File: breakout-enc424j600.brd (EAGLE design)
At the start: 58.4 x 33 mm, 25 parts, among them IC1 ENC424J600-I/PT, J1 HRJACK-HR911105A

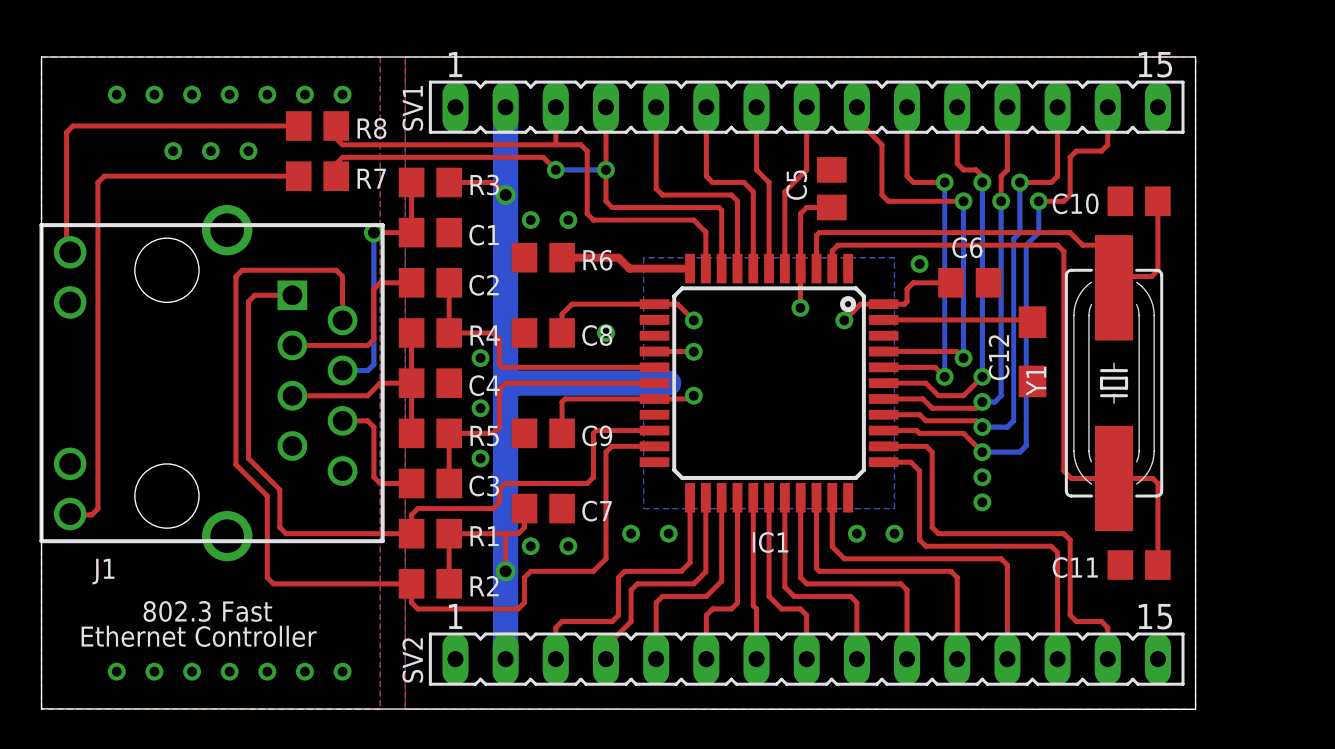
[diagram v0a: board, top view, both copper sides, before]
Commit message: Add pinout on silkscreen, change pin headers, connect ground shield on ethernet, modified board dimension
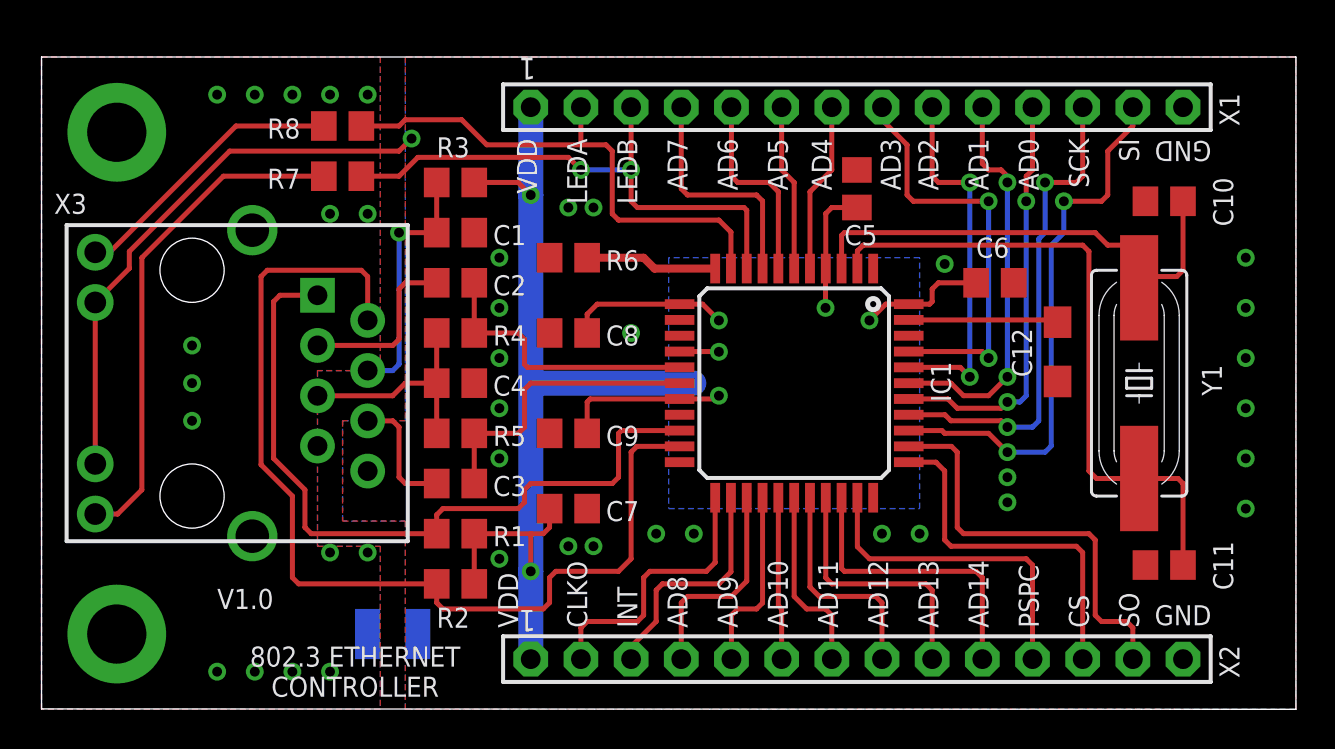
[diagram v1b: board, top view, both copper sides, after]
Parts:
- removed J1: HRJACK-HR911105A, various-electromechanical:HR911105A
- removed SV1, SV2: (no value), con-lsta:FE15
- added SJ1: (no value), jumper:SJW
- added X1, X2: TSW-114-07-G-S, con-samtec:TSW-114-XX-G-S
- added X3: HRJACK-SHIELD, various-electromechanical:HR911105A
- moved C10 1.27 mm to (56.8, 25.7)
- moved C11 1.27 mm to (56.8, 7.30)
- moved C12 1.27 mm to (51.4, 18.1)
- moved C7 1.27 mm to (26.7, 10.2)
- moved C8 1.27 mm to (26.7, 19.1)
- moved C9 1.27 mm to (26.7, 14.0)
- moved IC1 1.27 mm to (38.1, 16.5)
- moved R6 1.27 mm to (26.7, 22.9)
- moved Y1 1.27 mm to (55.6, 16.5)
- moved C1 1.27 mm to (21.0, 24.1)
- moved C2 1.27 mm to (21.0, 21.6)
- moved C3 1.27 mm to (21.0, 11.4)
- moved C4 1.27 mm to (21.0, 16.5)
- moved R1 1.27 mm to (21.0, 8.89)
- moved R2 1.27 mm to (21.0, 6.35)
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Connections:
- new net GNDIO: SJ1.1, X3.CGND@1, X3.CGND@2
- net AD0: now also X1.11; no longer SV1.12
- net AD1: now also X1.10; no longer SV1.11
- net AD10: now also X2.6; no longer SV2.7
- net AD11: now also X2.7; no longer SV2.8
- net AD12: now also X2.8; no longer SV2.9
- net AD13: now also X2.9; no longer SV2.10
- net AD14: now also X2.10; no longer SV2.11
- net AD2: now also X1.9; no longer SV1.10
- net AD3: now also X1.8; no longer SV1.9
- net AD4: now also X1.7; no longer SV1.8
- net AD5: now also X1.6; no longer SV1.7
- net AD6: now also X1.5; no longer SV1.6
- net AD7: now also X1.4; no longer SV1.5
- net AD8: now also X2.4; no longer SV2.5
- net AD9: now also X2.5; no longer SV2.6
- net CLKOUT: now also X2.2; no longer SV2.3
- net CS: now also X2.12; no longer SV2.13
- net GND: now also SJ1.2, X1.14, X2.14, X3.10, X3.11, X3.8; no longer J1.10, J1.11, J1.8, SV1.15, SV2.15
- net INT/SPISEL: now also X2.3; no longer SV2.4
- net LEDA: now also X1.2; no longer SV1.3
- net LEDB: now also X1.3; no longer SV1.4
- net N$2: now also X3.4; no longer J1.4
- net N$4: now also X3.3; no longer J1.3
- net N$5: now also X3.6; no longer J1.6
- net N$6: now also X3.5; no longer J1.5
- net N$8: now also X3.9; no longer J1.9
- net N$9: now also X3.12; no longer J1.12
- net PSPCFG0: now also X2.11; no longer SV2.12
- net SCK/AL: now also X1.12; no longer SV1.13
- net SI/RD/RW: now also X1.13; no longer SV1.14
- net SO/WR/EN: now also X2.13; no longer SV2.14
- net TPOUT+: now also X3.1; no longer J1.1
- net TPOUT-: now also X3.2; no longer J1.2
- net VDD: now also X1.1, X2.1; no longer SV1.2, SV2.2
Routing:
- net GND: track 0.00 -> 28.1 mm, vias 32 -> 25
- net N$8: track 18.0 -> 14.2 mm
- net N$9: track 28.4 -> 25.5 mm
- added copper zone on layer 1, net GNDIO
- added copper zone on layer 16, net GNDIO
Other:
- board size 58.4 x 33 mm -> 63.5 x 33 mm
- board text added: "802.3 ETHERNET CONTROLLER"
- board text added: "AD0"
- board text added: "AD1"
- board text added: "AD10"
- board text added: "AD11"
- board text added: "AD12"
- board text added: "AD13"
- board text added: "AD14"
- board text added: "AD2"
- board text added: "AD3"
- board text added: "AD4"
- board text added: "AD5"
- board text added: "AD6"
- board text added: "AD7"
- board text added: "AD8"
- board text added: "AD9"
- board text added: "CLKO"
- board text added: "CS"
- board text added: "GND"
- board text added: "INT"
- board text added: "LEDA"
- board text added: "LEDB"
- board text added: "PSPC"
- board text added: "SCK"
- board text added: "SI"
- board text added: "SO"
- board text added: "V1.0"
- board text added: "VDD"
- board text removed: "802.3 Fast"
- board text removed: "Ethernet Controller"

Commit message: Add missing component values
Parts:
- C10, C11: value 10 nF -> 20 pF
- C12: value (none) -> 10 uF
- R3: value (none) -> 10
- Y1: value (none) -> 25 MHz
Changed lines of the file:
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@@
 <?xml version="1.0" encoding="utf-8"?>
 <!DOCTYPE eagle SYSTEM "eagle.dtd">
-<eagle version="9.6.1">
+<eagle version="9.6.2">
 <drawing>
 <settings>
@@
 <attribute name="VALUE" x="20.32" y="3.81" size="1.016" layer="27" ratio="14"/>
 </element>
-<element name="R3" library="rcl" package="R0805" value="" x="20.955" y="26.67" smashed="yes">
+<element name="R3" library="rcl" package="R0805" value="10" x="20.955" y="26.67" smashed="yes">
 <attribute name="NAME" x="20.0025" y="27.94" size="1.016" layer="25" ratio="17"/>
 <attribute name="VALUE" x="20.32" y="24.13" size="1.27" layer="27"/>
@@
 <attribute name="VALUE" x="27.94" y="16.51" size="1.016" layer="27" ratio="14" rot="R180"/>
 </element>
-<element name="Y1" library="crystal" package="HC49UP" value="" x="55.5625" y="16.51" smashed="yes" rot="R90">
+<element name="Y1" library="crystal" package="HC49UP" value="25 MHz" x="55.5625" y="16.51" smashed="yes" rot="R90">
 <attribute name="NAME" x="59.7535" y="15.875" size="1.016" layer="25" ratio="14" rot="R90"/>
 <attribute name="VALUE" x="59.7535" y="10.795" size="1.27" layer="27" ratio="10" rot="R90"/>
 </element>
-<element name="C10" library="rcl" package="C0805" value="10 nF" x="56.8325" y="25.7175" smashed="yes">
+<element name="C10" library="rcl" package="C0805" value="20 pF" x="56.8325" y="25.7175" smashed="yes">
 <attribute name="NAME" x="60.325" y="24.4475" size="1.016" layer="25" ratio="14" rot="R90"/>
 <attribute name="VALUE" x="55.5625" y="23.1775" size="1.016" layer="27" ratio="14"/>
 </element>
-<element name="C11" library="rcl" package="C0805" value="10 nF" x="56.8325" y="7.3025" smashed="yes">
+<element name="C11" library="rcl" package="C0805" value="20 pF" x="56.8325" y="7.3025" smashed="yes">
 <attribute name="NAME" x="60.325" y="6.0325" size="1.016" layer="25" ratio="14" rot="R90"/>
 <attribute name="VALUE" x="55.5625" y="4.7625" size="1.016" layer="27" ratio="14"/>
@@
 <attribute name="VALUE" x="15.875" y="32.0675" size="1.016" layer="27" ratio="14" rot="R180"/>
 </element>
-<element name="C12" library="rcl" package="SMC_A" value="" x="51.435" y="18.0975" smashed="yes" rot="R270">
+<element name="C12" library="rcl" package="SMC_A" value="10 uF" x="51.435" y="18.0975" smashed="yes" rot="R270">
 <attribute name="NAME" x="50.1425" y="16.815" size="1.016" layer="25" ratio="14" rot="R90"/>
 <attribute name="VALUE" x="49.435" y="19.6975" size="1.016" layer="27" rot="R270"/>
